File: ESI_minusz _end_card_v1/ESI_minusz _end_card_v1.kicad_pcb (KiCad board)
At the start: 4 copper layers, 99.8 x 94.6 mm, 90 parts, among them J1 J-SAMTEC-TFM-120-01-L-D-RA, J2 U.FL-R-SMT-1, J3 M55-7101242R, J5 M55-7101242R, Q1 DMP2240UDM, Q2 PMV45EN, Q3 PMV45EN, Q4 PMV45EN, Q5 DMP2240UDM-7, Q6 PMV45EN, Q7 DMP2240UDM-7, U11 MIC842LYC5, U12 MIC842LYC5, U2 MAX7310, U201 TS5A21366, U202 TS5A21366, U203 TS5A21366, U204 TS5A21366

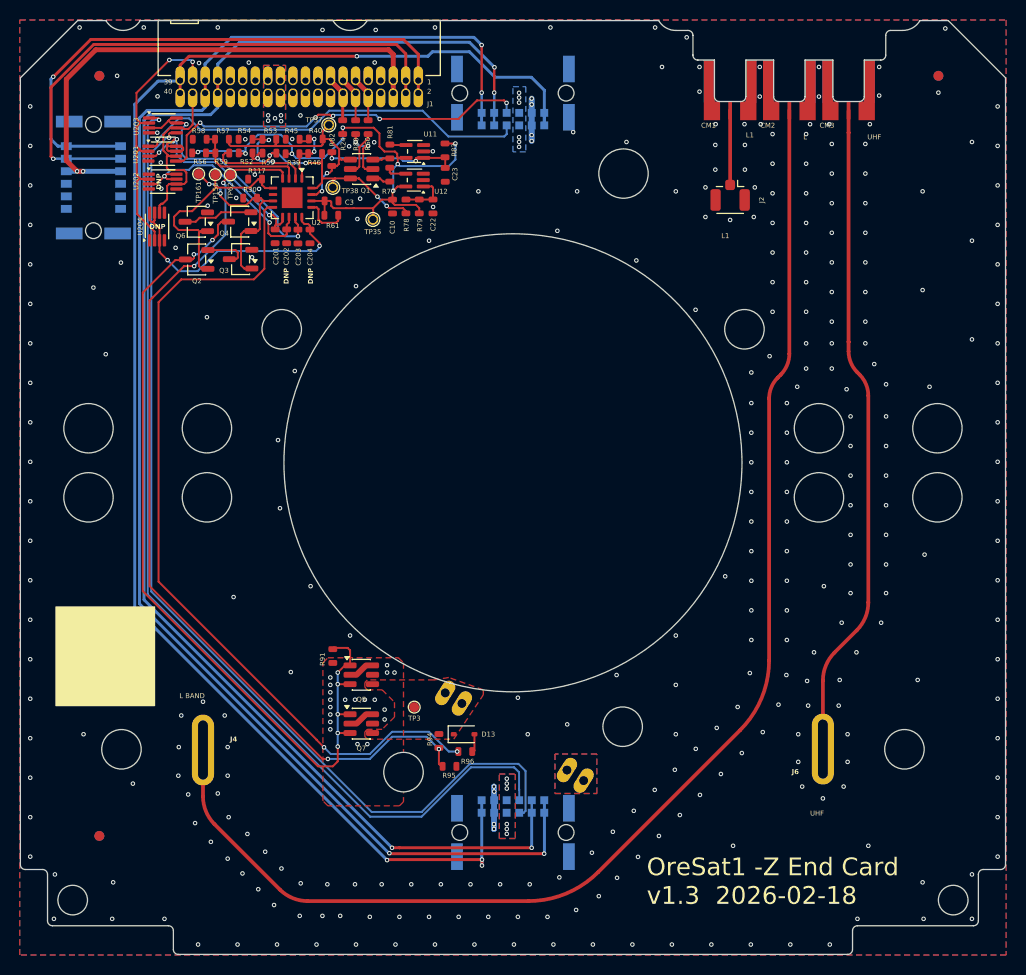
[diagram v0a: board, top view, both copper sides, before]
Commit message: Dipole schematic: added balun & footprints. Pre-tracing
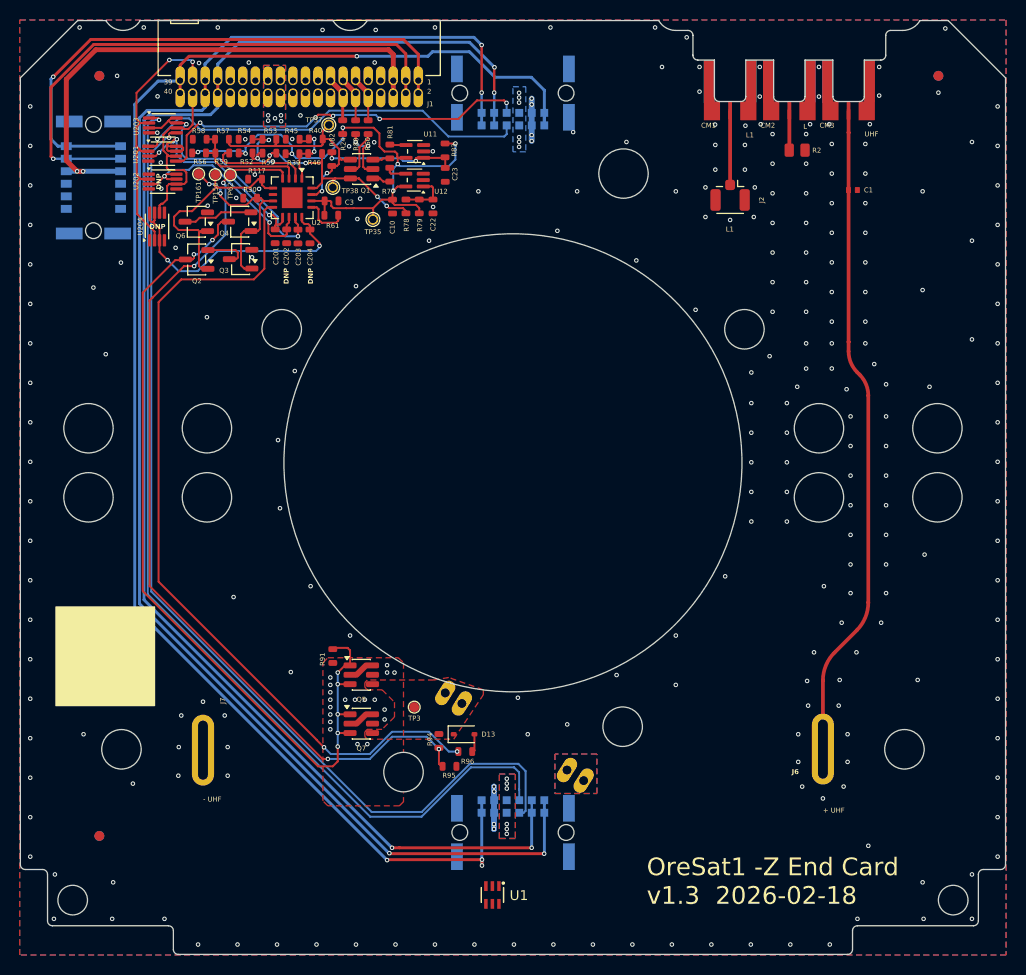
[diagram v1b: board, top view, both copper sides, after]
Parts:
- removed J4: ~, oresat-misc:tape-measure-slot-antenna
- added C1: 10p, oresat-passives:0402-C-NOSILK, F.Cu at (182.9, 74.9)
- added J7: -UHF, oresat-misc:tape-measure-slot-antenna, F.Cu at (117.1, 131.6)
- added R2: 50, oresat-passives:0805-C-NOSILK, F.Cu at (177.3, 70.8)
- added U1: NCS2-62+, oresat-passives:2450FB15A050E_JOT, F.Cu at (146.4, 146.3)
- J6: value ~ -> +UHF
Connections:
- J6 pad 1: /UHF -> /+UHF
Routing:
- net /LBAND: track 134.9 -> 4.03 mm
- net GND: vias 323 -> 260
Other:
- board text added: "+ UHF"
- board text added: "- UHF"

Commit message: Started RF tracing, not complete -- maybe need to move the balun b/c microstrip turns are too sharp
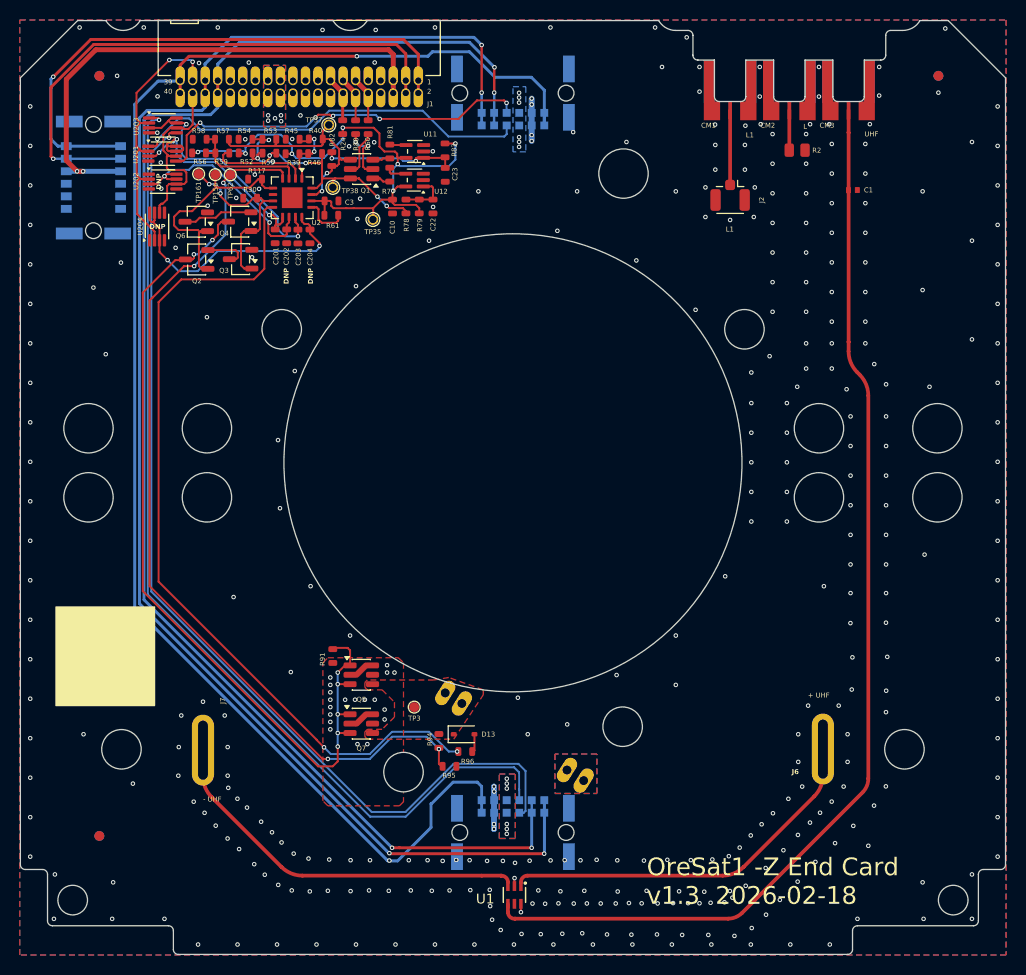
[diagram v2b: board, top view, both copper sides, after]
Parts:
- moved U1 2.23 mm to (148.7, 146.3)
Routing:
- net /UHF: track 66.8 -> 111.0 mm
- net /+UHF: track 0.00 -> 38.0 mm
- net /-UHF: track 0.00 -> 37.5 mm
- net GND: track 8.60 -> 10.3 mm, vias 260 -> 369
- net /~{SD}: track 157.2 -> 157.0 mm, vias 4 -> 1
